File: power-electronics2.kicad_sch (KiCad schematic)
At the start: 3 parts, among them U1 STP16NF06

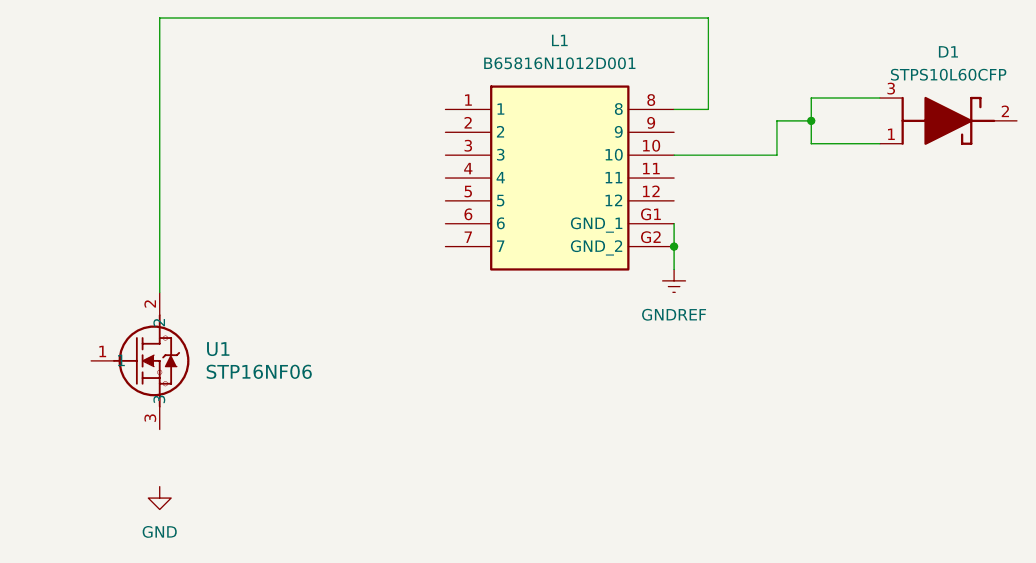
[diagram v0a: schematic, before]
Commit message: add some components
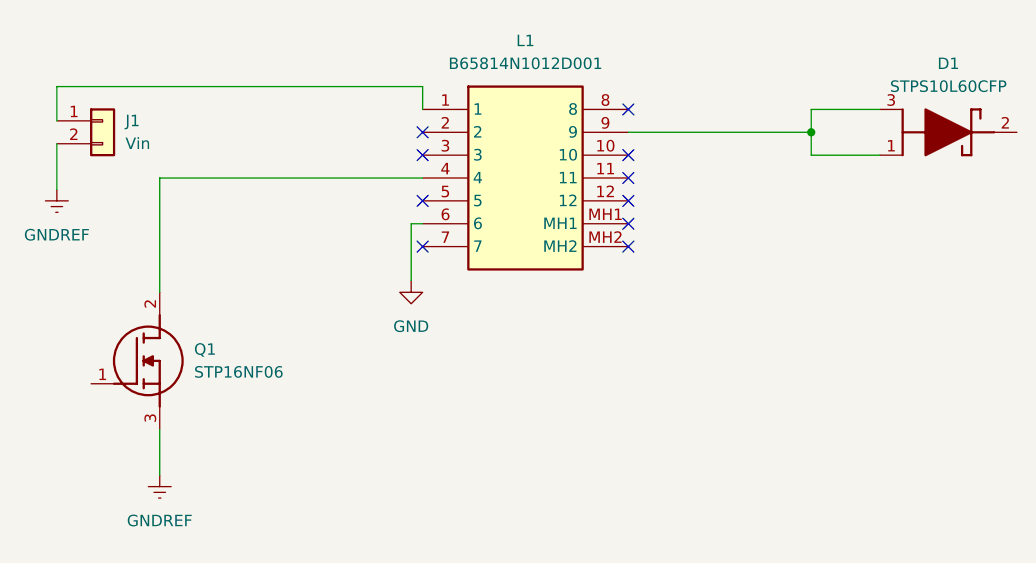
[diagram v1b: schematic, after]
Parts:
- removed L1: B65816N1012D001, Samacsys:B65816N1012D001, symbol Samacsys:B65816N1012D001
- removed U1: STP16NF06, Snapeda:TO-220_STM, symbol Snapeda:STP16NF06
- added J1: Vin, Connector_Wire:SolderWire-1.5sqmm_1x02_P6mm_D1.7mm_OD3mm, symbol Connector_Generic:Conn_01x02
- added L1: B65814N1012D001, Samacsys:B65814N1012D001, symbol Samacsys:B65814N1012D001
- added Q1: STP16NF06, Samacsys:TO270P460X1020X2008-3P, symbol Samacsys:STP16NF06
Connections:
- net GND: now also L1.6
- net GNDREF: now also J1.2 (Pin_2), Q1.3 (S)
- net at D1.1 (A1), D1.3 (A2): now also L1.9
- new net: J1.1 (Pin_1), L1.1
- new net: L1.4, Q1.2 (D)
- no-connect marks 0 -> 10

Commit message: add components
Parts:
- added IC1: UC2843BD1, Samacsys:SOIC127P600X175-8M, symbol Samacsys:UC2843BD1
- added IC2: ZTL431AFFTA, Samacsys:SOTFL95P240X110-3N, symbol Samacsys:ZTL431AFFTA
- added L2: B65816N1012D001, Samacsys:B65816N1012D001, symbol Samacsys:B65816N1012D001
- added U1: 4N35, Package_DIP:DIP-6_W7.62mm_SMDSocket_SmallPads, symbol Isolator:4N35
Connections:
- net GND: now also L1.7; no longer L1.6
- net GNDREF: now also IC1.5 (GROUND)
- net at L1.10: now also D1.1 (A1), D1.3 (A2), L1.9
- net at L1.3: now also L1.4, Q1.2 (D)
- net at Q1.1 (G): now also IC1.6 (OUTPUT)
- no-connect marks 10 -> 8
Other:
- moved on the sheet: J1

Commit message: finish pcb
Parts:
- removed L2: B65816N1012D001, Samacsys:B65816N1012D001, symbol Samacsys:B65816N1012D001
- added C1, C3: 47u, Capacitor_THT:CP_Radial_D10.0mm_P5.00mm, symbol Device:C_Polarized
- added C10: C, Capacitor_SMD:C_0805_2012Metric_Pad1.18x1.45mm_HandSolder, symbol Device:C
- added C11, C12: 1n8, Capacitor_SMD:C_0805_2012Metric_Pad1.18x1.45mm_HandSolder, symbol Device:C
- added C13: 1n6, Capacitor_SMD:C_0805_2012Metric_Pad1.18x1.45mm_HandSolder, symbol Device:C
- added C14: 1n, Capacitor_SMD:C_0805_2012Metric_Pad1.18x1.45mm_HandSolder, symbol Device:C
- added C15: u1, Capacitor_SMD:C_0805_2012Metric_Pad1.18x1.45mm_HandSolder, symbol Device:C
- added C16: 22u, Capacitor_SMD:C_0805_2012Metric_Pad1.18x1.45mm_HandSolder, symbol Device:C
- added C2: 3u3, Capacitor_THT:C_Axial_L12.0mm_D7.5mm_P15.00mm_Horizontal, symbol Device:C
- added C4: 390u, Capacitor_THT:CP_Radial_D10.0mm_P5.00mm, symbol Device:C_Polarized
- added C5: 1170u, Capacitor_THT:CP_Radial_D16.0mm_P7.50mm, symbol Device:C_Polarized
- added C6, C7, C8, C9: C, Capacitor_THT:CP_Radial_D10.0mm_P5.00mm, symbol Device:C_Polarized
- added D2: 1N4005, Diode_THT:D_DO-41_SOD81_P10.16mm_Horizontal, symbol Diode:1N4005
- added H1: B65816C1512T001, Samacsys:B65816C1512T001, symbol Samacsys:B65816C1512T001
- added IC4: LM317LD, Samacsys:SOIC127P600X175-8N, symbol Samacsys:LM317LD
- added J2: Vo, Connector_Wire:SolderWire-1.5sqmm_1x02_P6mm_D1.7mm_OD3mm, symbol Connector_Generic:Conn_01x02
- added L3: 123u, Inductor_THT:L_Axial_L29.9mm_D14.0mm_P38.00mm_Horizontal_Vishay_IHA-105, symbol Device:L
- added L4: 470u, Inductor_THT:L_Axial_L29.9mm_D14.0mm_P38.00mm_Horizontal_Vishay_IHA-105, symbol Device:L
- added Q2: 2N3906, Package_TO_SOT_THT:TO-92_Inline, symbol Transistor_BJT:2N3906
- added R1: 445m, Resistor_SMD:R_0805_2012Metric_Pad1.20x1.40mm_HandSolder, symbol Device:R
- added R10, R12: 10k, Resistor_SMD:R_0805_2012Metric_Pad1.20x1.40mm_HandSolder, symbol Device:R
- added R11: 12k3, Resistor_SMD:R_0805_2012Metric_Pad1.20x1.40mm_HandSolder, symbol Device:R
- added R13: 2k7, Resistor_SMD:R_0805_2012Metric_Pad1.20x1.40mm_HandSolder, symbol Device:R
- added R14: 240R, Resistor_SMD:R_0805_2012Metric_Pad1.20x1.40mm_HandSolder, symbol Device:R
- added R15: 50k, Resistor_SMD:R_0805_2012Metric_Pad1.20x1.40mm_HandSolder, symbol Device:R
- added R2, R3, R4: R, Resistor_SMD:R_0805_2012Metric_Pad1.20x1.40mm_HandSolder, symbol Device:R
- added R5: 10R, Resistor_SMD:R_0805_2012Metric_Pad1.20x1.40mm_HandSolder, symbol Device:R
- added R6: WSR5R1000FEA, Samacsys:RESM11670X254N, symbol Samacsys:WSR5R1000FEA
- added R7, R8: CRA2512-FZ-R050ELF, Samacsys:RESC6434X90N, symbol Samacsys:CRA2512-FZ-R050ELF
- added R9: 100R, Resistor_SMD:R_0805_2012Metric_Pad1.20x1.40mm_HandSolder, symbol Device:R
- added VR1: PTV09A-4020F-B104, Samacsys:PTV09A4020FB103, symbol Samacsys:PTV09A-4020F-B104
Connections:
- net GND: now also IC2.1 (ANODE), L1.12, C1.2, C2.2, C3.2, H1.10, H1.3, J2.2 (Pin_2), R3.2
- net GNDREF: now also U1.4, C11.2, C12.2, C13.2, C15.2, C16.2, C4.2, C5.2, C6.2, C7.2, C8.2, C9.2, Q2.3 (C), R13.2, R6.1; no longer Q1.3 (S)
- net Vi: now reaches J1.1 (Pin_1)
- net Vi: now also C15.1, IC4.1 (VIN), L4.1, R1.1; no longer L1.1
- net Vs+: now reaches D1.1 (A1), D1.3 (A2)
- net Vs+: now also L1.11, H1.2; no longer L1.10, L1.9
- net Vp+: now reaches L1.2
- net Vp+: now also C5.1, C8.1, C9.1, H1.5, L3.2
- net at L1.5: now also H1.8
- net Vp-: now reaches L1.6
- net Vp-: now also L1.1, Q1.2 (D), H1.4, H1.9
- net at L1.8: now also H1.11
- net at Q1.1 (G): now also R5.2; no longer IC1.6 (OUTPUT)
- net at IC2.2 (REF): now also C10.2, VR1.2 (WIPER)
- net at IC2.3 (CATHODE): now also U1.2, C10.1
- net at IC1.1 (COMP): now also C14.1, R12.1
- net at IC1.2 (VFB): now also U1.5, C13.1, C14.2, R11.2, R12.2
- net at IC1.3 (ISENSE): now also C11.1, R9.1
- net at IC1.4 (RT/CT): now also C12.1, R10.2
- net Vldo: now reaches IC1.7 (VI)
- net Vldo: now also D2.1 (K), IC4.2 (VOUT_1), IC4.3 (VOUT_2), IC4.6 (VOUT_3), IC4.7 (VOUT_4), R11.1, R14.2, R15.2
- net at IC1.8 (VREF): now also R10.1
- net Vo: now reaches D1.2 (K)
- net Vo: now also C1.1, C2.1, C3.1, J2.1 (Pin_1), R2.1, R4.1
- net at U1.1: now also R4.2
- new net: IC4.4 (ADJ), Q2.1 (E), R13.1, R14.1, R15.1
- new net: C4.1, C6.1, C7.1, L3.1, L4.2, R1.2
- new net: Q1.3 (S), R7.2, R8.2, R9.2
- new net: R6.2, R7.1, R8.1
- new net: C16.1, D2.2 (A), Q2.2 (B)
- new net: R2.2, VR1.1 (CCW)
- new net: R3.1, VR1.3 (CW)
- new net: IC1.6 (OUTPUT), R5.1
- new net: H1.1, L1.10
- new net: H1.12, L1.9
- new net: H1.6, L1.3
- new net: H1.7, L1.4
- no-connect marks 8 -> 5
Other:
- moved on the sheet: D1, IC1, IC2, J1, Q1, U1
